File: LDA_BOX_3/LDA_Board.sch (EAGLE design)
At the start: 65 parts, among them IC1 STM32F407ZET, SW3P-2 LD-CCB-001, Y1 8MHZ

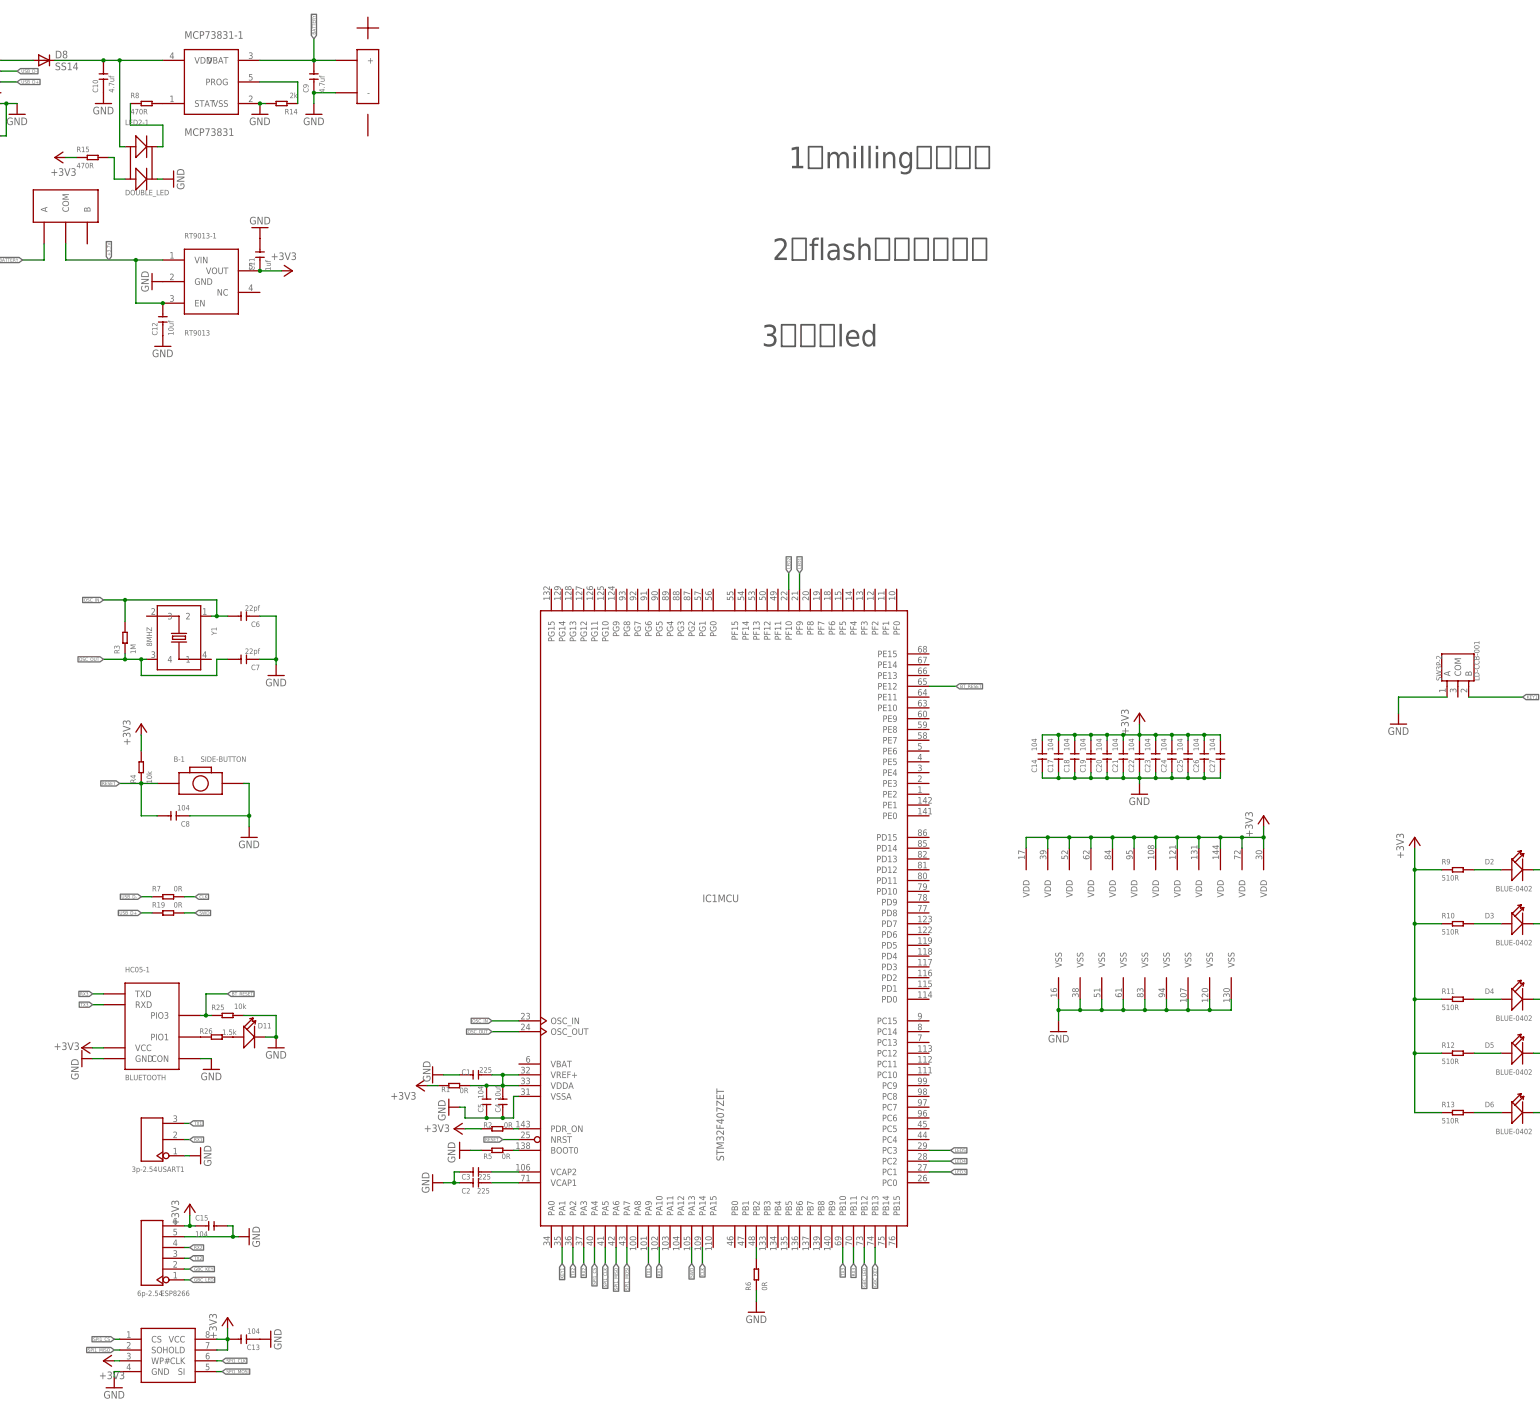
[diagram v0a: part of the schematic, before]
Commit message: 第三版盒子，丝印加了logo
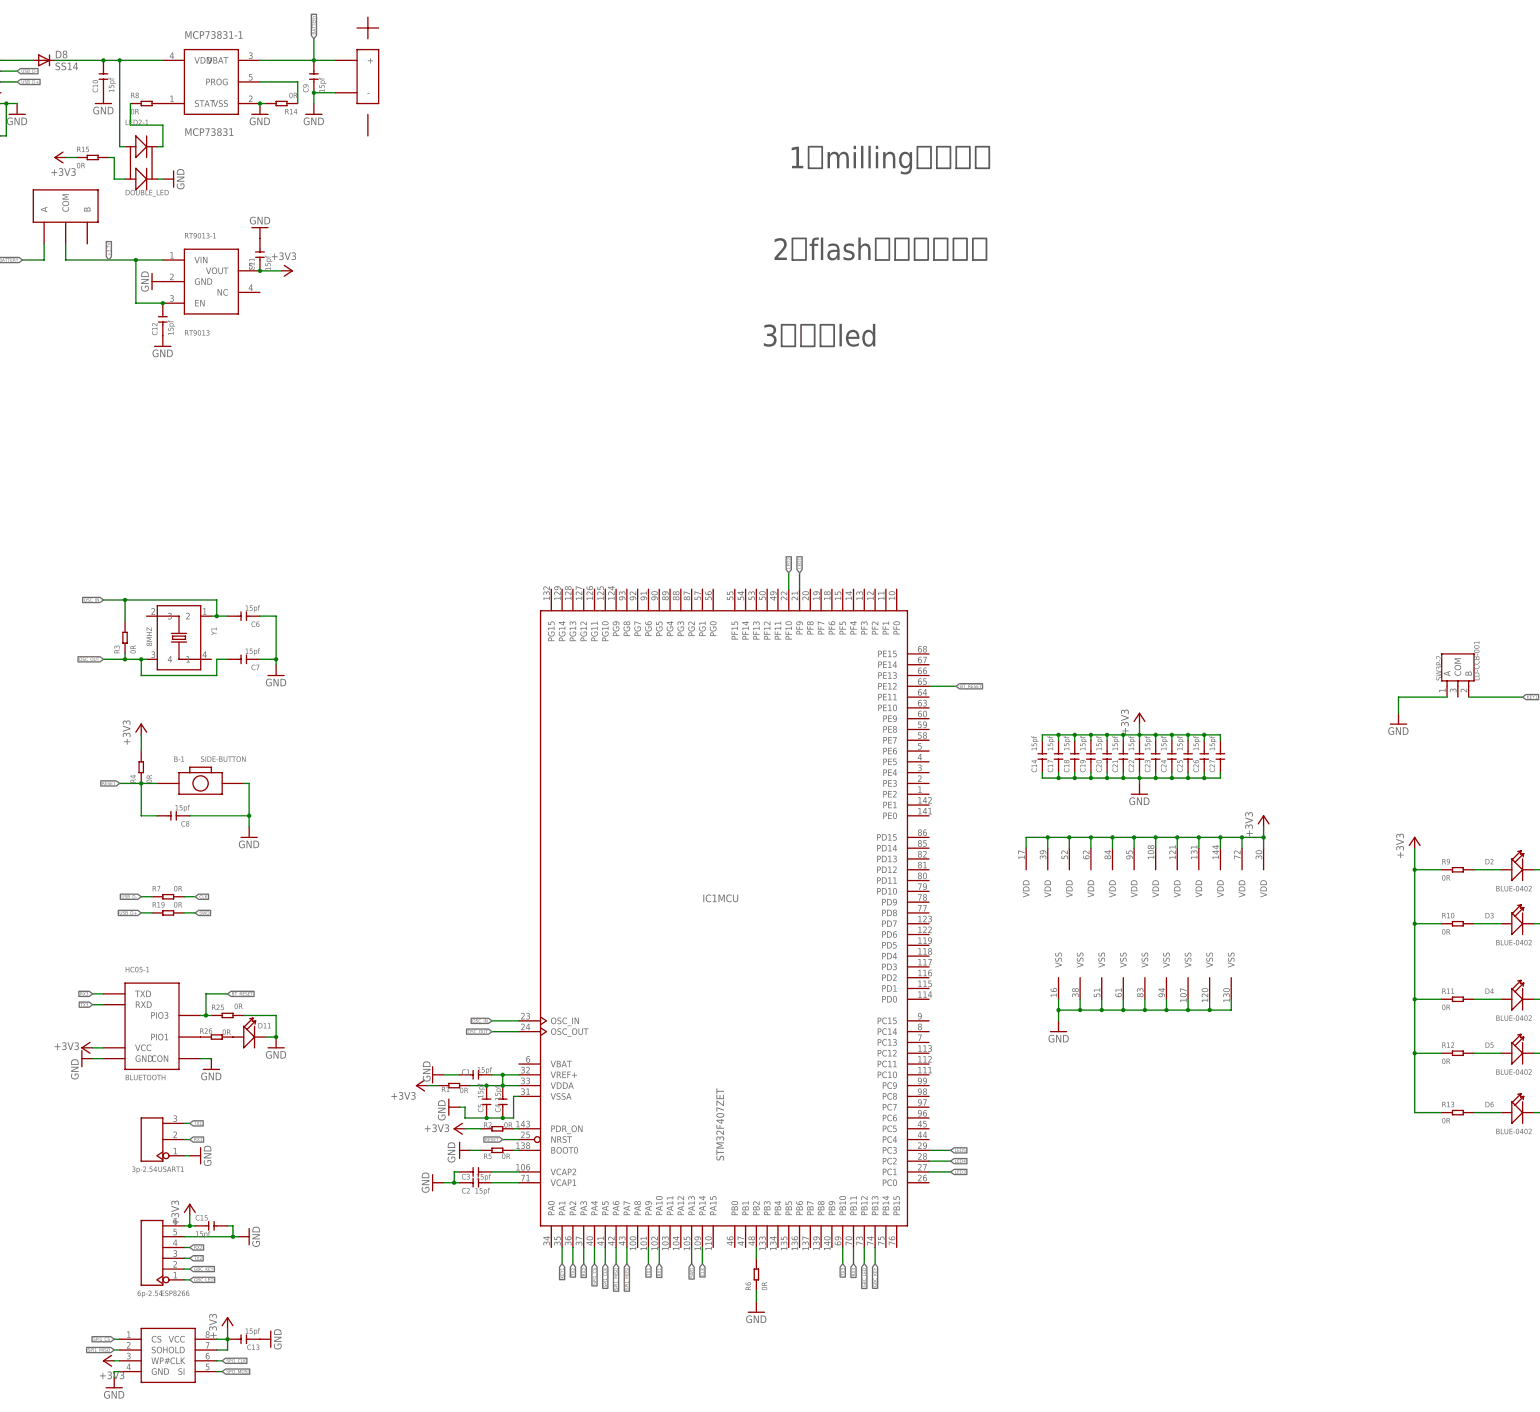
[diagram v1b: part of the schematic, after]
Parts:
- C1, C2, C3: value 225 -> 15pf
- C10, C9: value 4.7uf -> 15pf
- C11: value 1uf -> 15pf
- C12, C4: value 10uf -> 15pf
- C13, C14, C15, C17, C18, C19, C20, C21, C22, C23, C24, C25, C26, C27, C5, C8: value 104 -> 15pf
- C6, C7: value 22pf -> 15pf
- R10, R11, R12, R13, R9: value 510R -> 0R
- R14: value 2k -> 0R
- R15, R8: value 470R -> 0R
- R25, R4: value 10k -> 0R
- R26: value 1.5k -> 0R
- R3: value 1M -> 0R
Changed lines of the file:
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@@
 <part name="USB2" library="1-LDA_Board" deviceset="MICRO-USB-SMD(ZX62-B-5PA)" device="" value="ZX62-B-5PA"/>
 <part name="MCP73831-1" library="1-LDA_Board" deviceset="MCP73831" device=""/>
-<part name="C9" library="1-LDA_Board" deviceset="CAP-(0402)" device="" value="4.7uf"/>
-<part name="C10" library="1-LDA_Board" deviceset="CAP-(0402)" device="" value="4.7uf"/>
-<part name="R8" library="1-LDA_Board" deviceset="RES-(0402)" device="" value="470R"/>
-<part name="R14" library="1-LDA_Board" deviceset="RES-(0402)" device="" value="2k"/>
+<part name="C9" library="1-LDA_Board" deviceset="CAP-(0402)" device="" value="15pf"/>
+<part name="C10" library="1-LDA_Board" deviceset="CAP-(0402)" device="" value="15pf"/>
+<part name="R8" library="1-LDA_Board" deviceset="RES-(0402)" device="" value="0R"/>
+<part name="R14" library="1-LDA_Board" deviceset="RES-(0402)" device="" value="0R"/>
 <part name="GND10" library="1-LDA_Board" deviceset="GND" device=""/>
 <part name="GND11" library="1-LDA_Board" deviceset="GND" device=""/>
@@
 <part name="GND23" library="1-LDA_Board" deviceset="GND" device=""/>
 <part name="RT9013-1" library="1-LDA_Board" deviceset="RT9013" device=""/>
-<part name="C11" library="1-LDA_Board" deviceset="CAP-(0402)" device="" value="1uf"/>
-<part name="C12" library="1-LDA_Board" deviceset="CAP-(0402)" device="" value="10uf"/>
+<part name="C11" library="1-LDA_Board" deviceset="CAP-(0402)" device="" value="15pf"/>
+<part name="C12" library="1-LDA_Board" deviceset="CAP-(0402)" device="" value="15pf"/>
 <part name="GND24" library="1-LDA_Board" deviceset="GND" device=""/>
 <part name="GND25" library="1-LDA_Board" deviceset="GND" device=""/>
 <part name="GND26" library="1-LDA_Board" deviceset="GND" device=""/>
 <part name="+3V5" library="1-LDA_Board" deviceset="+3V3" device=""/>
-<part name="C14" library="1-LDA_Board" deviceset="CAP-(0402)" device="" value="104"/>
-<part name="C17" library="1-LDA_Board" deviceset="CAP-(0402)" device="" value="104"/>
-<part name="C18" library="1-LDA_Board" deviceset="CAP-(0402)" device="" value="104"/>
-<part name="C19" library="1-LDA_Board" deviceset="CAP-(0402)" device="" value="104"/>
-<part name="C20" library="1-LDA_Board" deviceset="CAP-(0402)" device="" value="104"/>
-<part name="C21" library="1-LDA_Board" deviceset="CAP-(0402)" device="" value="104"/>
-<part name="C22" library="1-LDA_Board" deviceset="CAP-(0402)" device="" value="104"/>
-<part name="C23" library="1-LDA_Board" deviceset="CAP-(0402)" device="" value="104"/>
-<part name="C24" library="1-LDA_Board" deviceset="CAP-(0402)" device="" value="104"/>
-<part name="C25" library="1-LDA_Board" deviceset="CAP-(0402)" device="" value="104"/>
-<part name="C26" library="1-LDA_Board" deviceset="CAP-(0402)" device="" value="104"/>
-<part name="C27" library="1-LDA_Board" deviceset="CAP-(0402)" device="" value="104"/>
-<part name="C1" library="1-LDA_Board" deviceset="CAP-(0402)" device="" value="225"/>
-<part name="C4" library="1-LDA_Board" deviceset="CAP-(0402)" device="" value="10uf"/>
-<part name="C5" library="1-LDA_Board" deviceset="CAP-(0402)" device="" value="104"/>
-<part name="C2" library="1-LDA_Board" deviceset="CAP-(0402)" device="" value="225"/>
-<part name="C3" library="1-LDA_Board" deviceset="CAP-(0402)" device="" value="225"/>
+<part name="C14" library="1-LDA_Board" deviceset="CAP-(0402)" device="" value="15pf"/>
+<part name="C17" library="1-LDA_Board" deviceset="CAP-(0402)" device="" value="15pf"/>
+<part name="C18" library="1-LDA_Board" deviceset="CAP-(0402)" device="" value="15pf"/>
+<part name="C19" library="1-LDA_Board" deviceset="CAP-(0402)" device="" value="15pf"/>
+<part name="C20" library="1-LDA_Board" deviceset="CAP-(0402)" device="" value="15pf"/>
+<part name="C21" library="1-LDA_Board" deviceset="CAP-(0402)" device="" value="15pf"/>
+<part name="C22" library="1-LDA_Board" deviceset="CAP-(0402)" device="" value="15pf"/>
+<part name="C23" library="1-LDA_Board" deviceset="CAP-(0402)" device="" value="15pf"/>
+<part name="C24" library="1-LDA_Board" deviceset="CAP-(0402)" device="" value="15pf"/>
+<part name="C25" library="1-LDA_Board" deviceset="CAP-(0402)" device="" value="15pf"/>
+<part name="C26" library="1-LDA_Board" deviceset="CAP-(0402)" device="" value="15pf"/>
+<part name="C27" library="1-LDA_Board" deviceset="CAP-(0402)" device="" value="15pf"/>
+<part name="C1" library="1-LDA_Board" deviceset="CAP-(0402)" device="" value="15pf"/>
+<part name="C4" library="1-LDA_Board" deviceset="CAP-(0402)" device="" value="15pf"/>
+<part name="C5" library="1-LDA_Board" deviceset="CAP-(0402)" device="" value="15pf"/>
+<part name="C2" library="1-LDA_Board" deviceset="CAP-(0402)" device="" value="15pf"/>
+<part name="C3" library="1-LDA_Board" deviceset="CAP-(0402)" device="" value="15pf"/>
 <part name="R1" library="1-LDA_Board" deviceset="RES-(0402)" device="" value="0R"/>
 <part name="R2" library="1-LDA_Board" deviceset="RES-(0402)" device="" value="0R"/>
 <part name="R5" library="1-LDA_Board" deviceset="RES-(0402)" device="" value="0R"/>
 <part name="R6" library="1-LDA_Board" deviceset="RES-(0402)" device="" value="0R"/>
-<part name="R3" library="1-LDA_Board" deviceset="RES-(0402)" device="" value="1M"/>
-<part name="C6" library="1-LDA_Board" deviceset="CAP-(0402)" device="" value="22pf"/>
-<part name="C7" library="1-LDA_Board" deviceset="CAP-(0402)" device="" value="22pf"/>
-<part name="R4" library="1-LDA_Board" deviceset="RES-(0402)" device="" value="10k"/>
-<part name="C8" library="1-LDA_Board" deviceset="CAP-(0402)" device="" value="104"/>
-<part name="C13" library="1-LDA_Board" deviceset="CAP-(0402)" device="" value="104"/>
+<part name="R3" library="1-LDA_Board" deviceset="RES-(0402)" device="" value="0R"/>
+<part name="C6" library="1-LDA_Board" deviceset="CAP-(0402)" device="" value="15pf"/>
+<part name="C7" library="1-LDA_Board" deviceset="CAP-(0402)" device="" value="15pf"/>
+<part name="R4" library="1-LDA_Board" deviceset="RES-(0402)" device="" value="0R"/>
+<part name="C8" library="1-LDA_Board" deviceset="CAP-(0402)" device="" value="15pf"/>
+<part name="C13" library="1-LDA_Board" deviceset="CAP-(0402)" device="" value="15pf"/>
 <part name="D8" library="1-LDA_Board" deviceset="SS14" device=""/>
 <part name="HC05-1" library="1-LDA_Board" deviceset="BLUETOOTH" device=""/>
@@
 <part name="+3V8" library="1-LDA_Board" deviceset="+3V3" device=""/>
 <part name="BATTERY-1" library="1-LDA_Board" deviceset="BATTERY" device=""/>
-<part name="R9" library="1-LDA_Board" deviceset="RES-(0402)" device="" value="510R"/>
-<part name="R10" library="1-LDA_Board" deviceset="RES-(0402)" device="" value="510R"/>
-<part name="R11" library="1-LDA_Board" deviceset="RES-(0402)" device="" value="510R"/>
-<part name="R12" library="1-LDA_Board" deviceset="RES-(0402)" device="" value="510R"/>
-<part name="R13" library="1-LDA_Board" deviceset="RES-(0402)" device="" value="510R"/>
+<part name="R9" library="1-LDA_Board" deviceset="RES-(0402)" device="" value="0R"/>
+<part name="R10" library="1-LDA_Board" deviceset="RES-(0402)" device="" value="0R"/>
+<part name="R11" library="1-LDA_Board" deviceset="RES-(0402)" device="" value="0R"/>
+<part name="R12" library="1-LDA_Board" deviceset="RES-(0402)" device="" value="0R"/>
+<part name="R13" library="1-LDA_Board" deviceset="RES-(0402)" device="" value="0R"/>
 <part name="D2" library="1-LDA_Board" deviceset="LED-(0402)" device="" value="BLUE-0402"/>
 <part name="D3" library="1-LDA_Board" deviceset="LED-(0402)" device="" value="BLUE-0402"/>
@@
 <part name="D5" library="1-LDA_Board" deviceset="LED-(0402)" device="" value="BLUE-0402"/>
 <part name="D6" library="1-LDA_Board" deviceset="LED-(0402)" device="" value="BLUE-0402"/>
-<part name="C15" library="1-LDA_Board" deviceset="CAP-(0402)" device="" value="104"/>
+<part name="C15" library="1-LDA_Board" deviceset="CAP-(0402)" device="" value="15pf"/>
 <part name="SW3P-2" library="1-LDA_Board" deviceset="SWITCH(3P)" device="" value="LD-CCB-001"/>
 <part name="SW-1" library="1-LDA_Board" deviceset="SWITCH-3P" device=""/>
 <part name="B-1" library="1-LDA_Board" deviceset="SIDE-BUTTON" device=""/>
-<part name="R25" library="1-LDA_Board" deviceset="RES-(0402)" device="" value="10k"/>
-<part name="R26" library="1-LDA_Board" deviceset="RES-(0402)" device="" value="1.5k"/>
+<part name="R25" library="1-LDA_Board" deviceset="RES-(0402)" device="" value="0R"/>
+<part name="R26" library="1-LDA_Board" deviceset="RES-(0402)" device="" value="0R"/>
 <part name="D11" library="1-LDA_Board" deviceset="LED-(0402)" device="" value="BLUE-0402"/>
 <part name="GND18" library="1-LDA_Board" deviceset="GND" device=""/>
@@
 <part name="GND13" library="1-LDA_Board" deviceset="GND" device=""/>
 <part name="+3V6" library="1-LDA_Board" deviceset="+3V3" device=""/>
-<part name="R15" library="1-LDA_Board" deviceset="RES-(0402)" device="" value="470R"/>
+<part name="R15" library="1-LDA_Board" deviceset="RES-(0402)" device="" value="0R"/>
 </parts>
 <sheets>
